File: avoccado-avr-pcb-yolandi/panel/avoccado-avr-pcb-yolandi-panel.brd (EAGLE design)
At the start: 100 x 100.5 mm, 784 parts, among them Q1 16MHz, Q10 FET, Q11 16MHz, Q12 FET, Q13 16MHz, Q14 FET, Q15 16MHz, Q16 FET, Q17 16MHz, Q18 FET, Q19 16MHz, Q2 FET, Q20 FET, Q21 16MHz, Q22 FET, Q23 16MHz, Q24 FET, Q25 16MHz, Q26 FET, Q27 16MHz, Q28 FET, Q29 16MHz, Q3 16MHz, Q30 FET, Q31 16MHz, Q32 FET, Q4 FET, Q5 16MHz, Q6 FET, Q7 16MHz, Q8 FET, Q9 16MHz, U1 MCP73831, U10 MCP73831, U11 MCP73831, U12 MCP73831, U13 MCP73831, U14 MCP73831, U15 MCP73831, U16 MCP73831, U2 MCP73831, U3 MCP73831, U4 MCP73831, U5 MCP73831, U6 MCP73831, U7 MCP73831, U8 MCP73831, U9 MCP73831

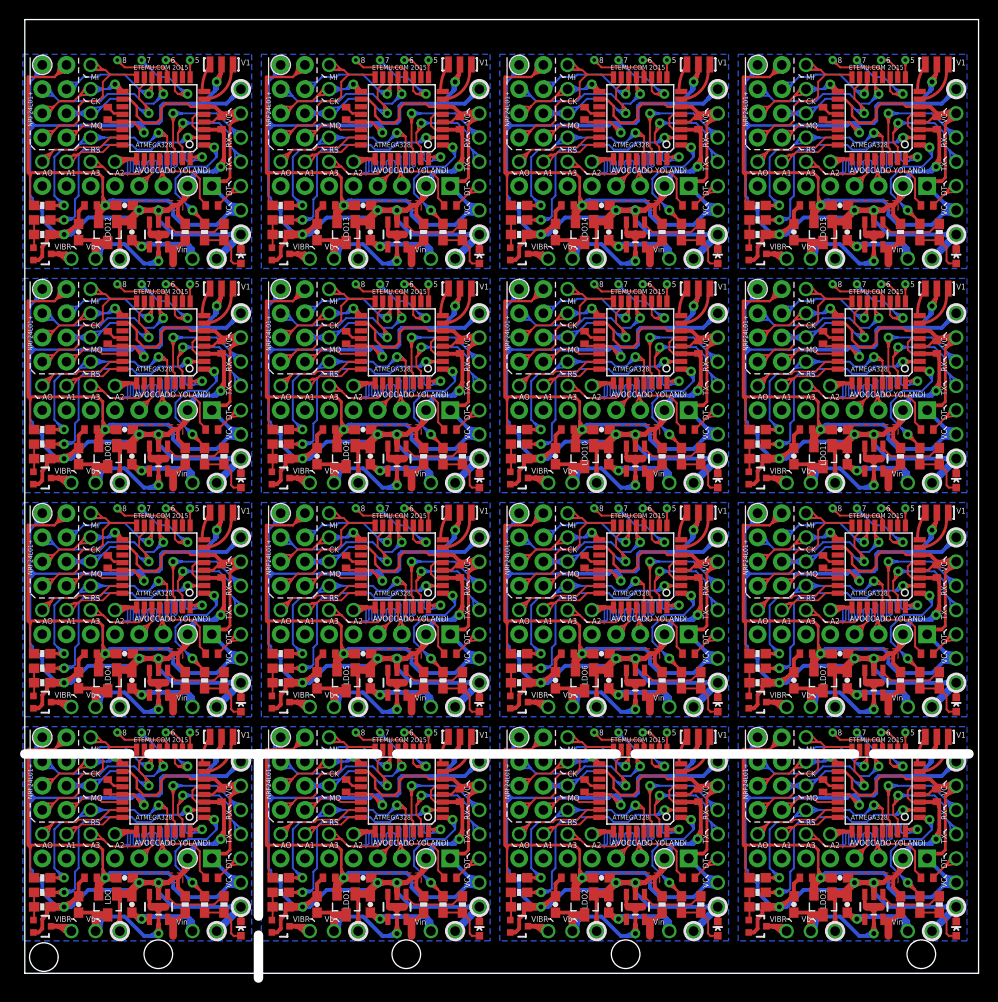
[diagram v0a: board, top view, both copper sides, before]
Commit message: Nora: new PCB with plated half holes for surface mounting
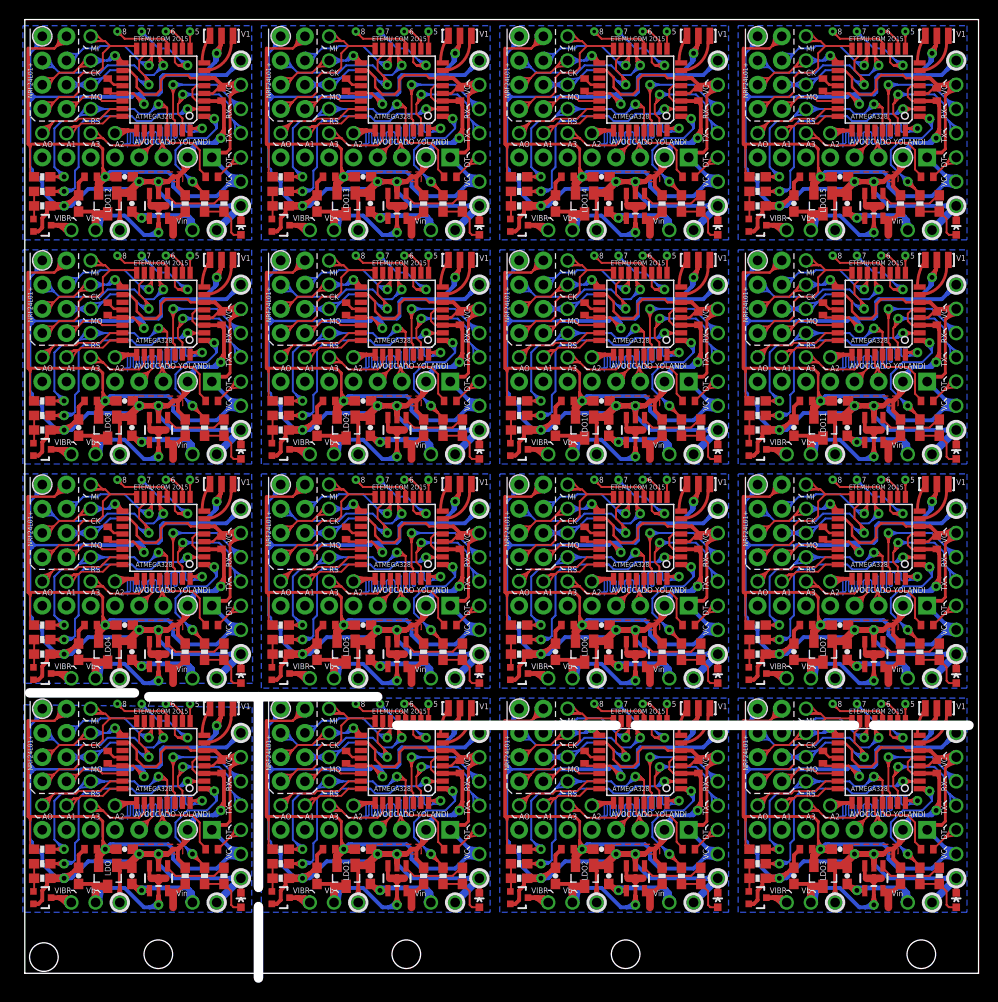
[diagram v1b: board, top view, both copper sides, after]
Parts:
- moved C32 3.00 mm to (11.2, 33.7)
- moved C34 3.00 mm to (5.64, 33.7)
- moved C39 3.00 mm to (36.2, 33.7)
- moved C41 3.00 mm to (30.6, 33.7)
- moved C46 3.00 mm to (61.2, 33.7)
- moved C48 3.00 mm to (55.6, 33.7)
- moved C53 3.00 mm to (86.2, 33.7)
- moved C55 3.00 mm to (80.6, 33.7)
- moved LDO4 3.00 mm to (8.69, 33.7)
- moved LDO5 3.00 mm to (33.7, 33.7)
- moved LDO6 3.00 mm to (58.7, 33.7)
- moved LDO7 3.00 mm to (83.7, 33.7)
- moved R27 3.00 mm to (16.8, 33.7)
- moved R28 3.00 mm to (20.9, 33.7)
- moved R30 3.00 mm to (18.9, 33.7)
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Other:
- outline, holes or cut-outs redrawn

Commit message: panelized nora to 50x50mm²
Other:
- board size 100 x 100.5 mm -> 100.1 x 100.5 mm
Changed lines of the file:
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@@
 <hole x="63" y="2" drill="3"/>
 <hole x="94" y="2" drill="3"/>
+<wire x1="-0.1" y1="76.5" x2="27.9" y2="76.5" width="1" layer="46"/>
+<wire x1="24.5" y1="70" x2="24.5" y2="83" width="1" layer="46"/>
 </plain>
 <attributes>
